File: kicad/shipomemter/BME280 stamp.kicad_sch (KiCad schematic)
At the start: 7 parts, among them U1 BME280

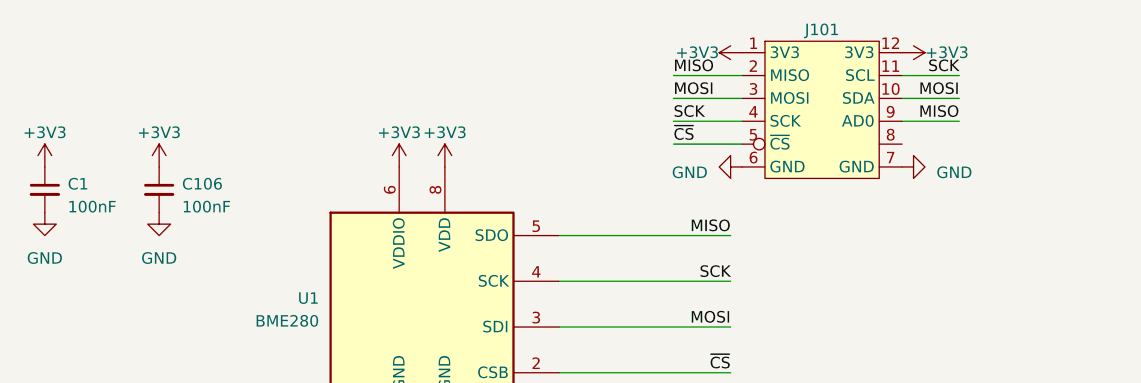
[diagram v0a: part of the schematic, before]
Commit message: Pulled in ICM20948
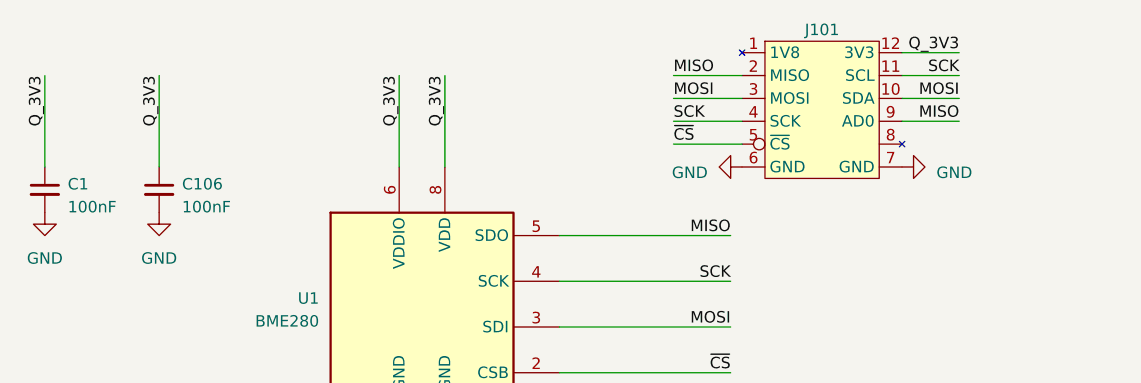
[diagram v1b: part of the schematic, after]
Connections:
- net +3V3 renamed Q_3V3
- net Q_3V3: no longer J101.1 (3V3)

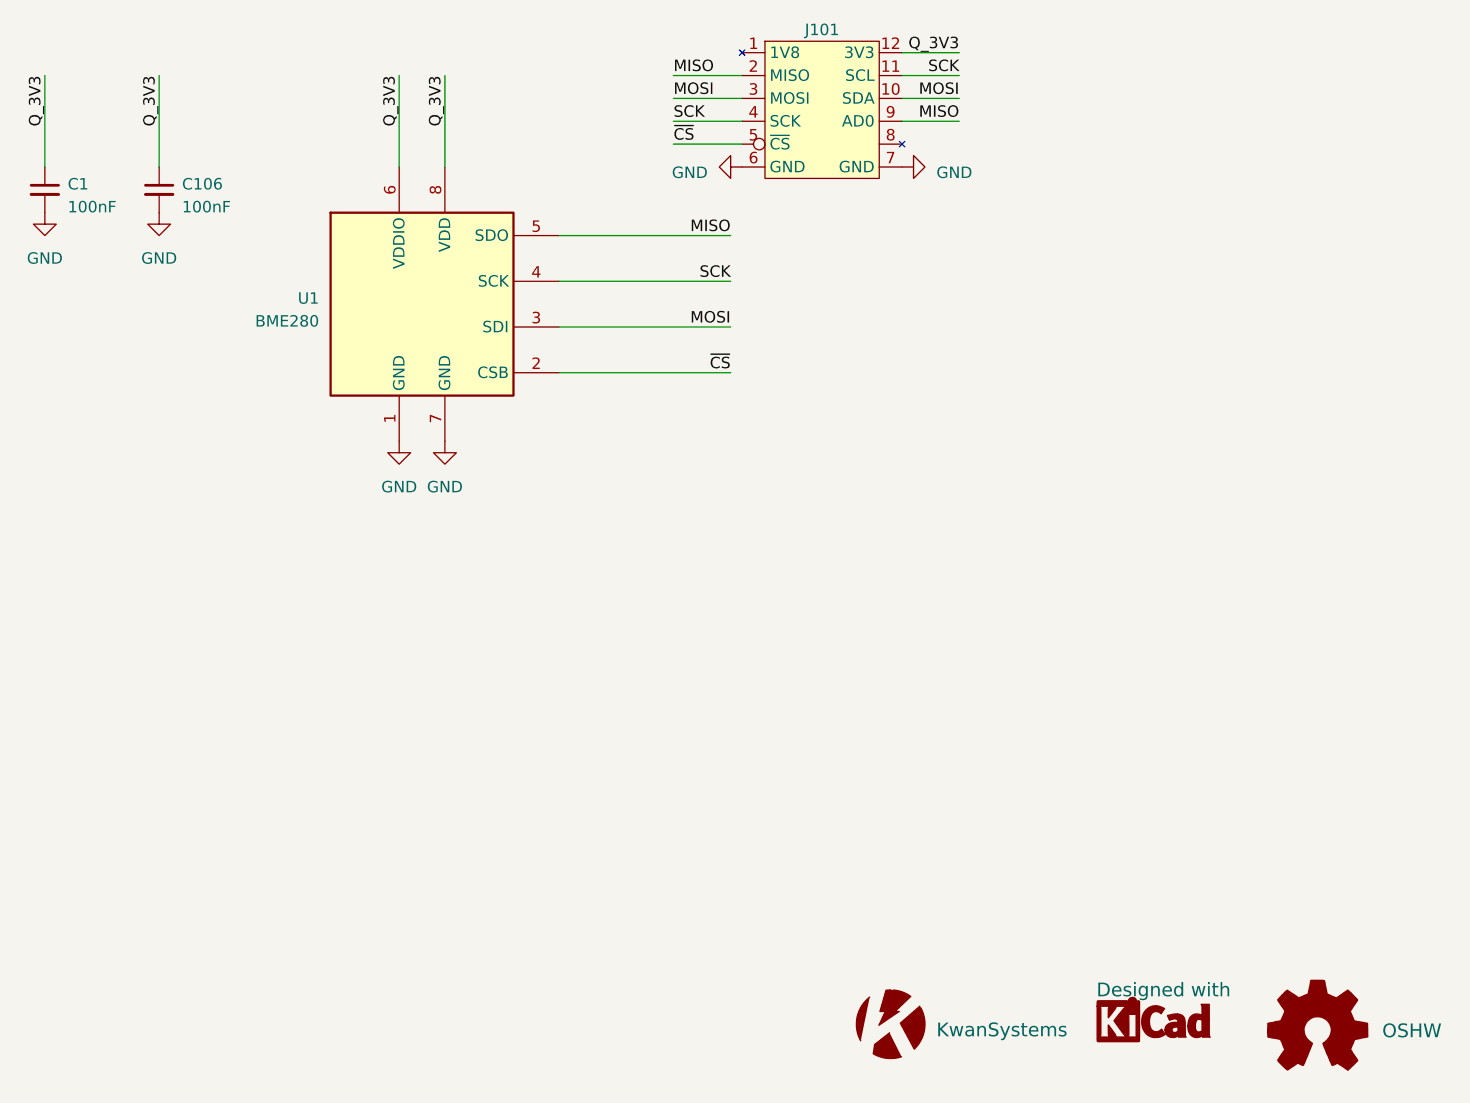
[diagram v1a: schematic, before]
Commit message: As ordered on 03 Apr 2023. Some but not all numbers-on-hand have been updated.
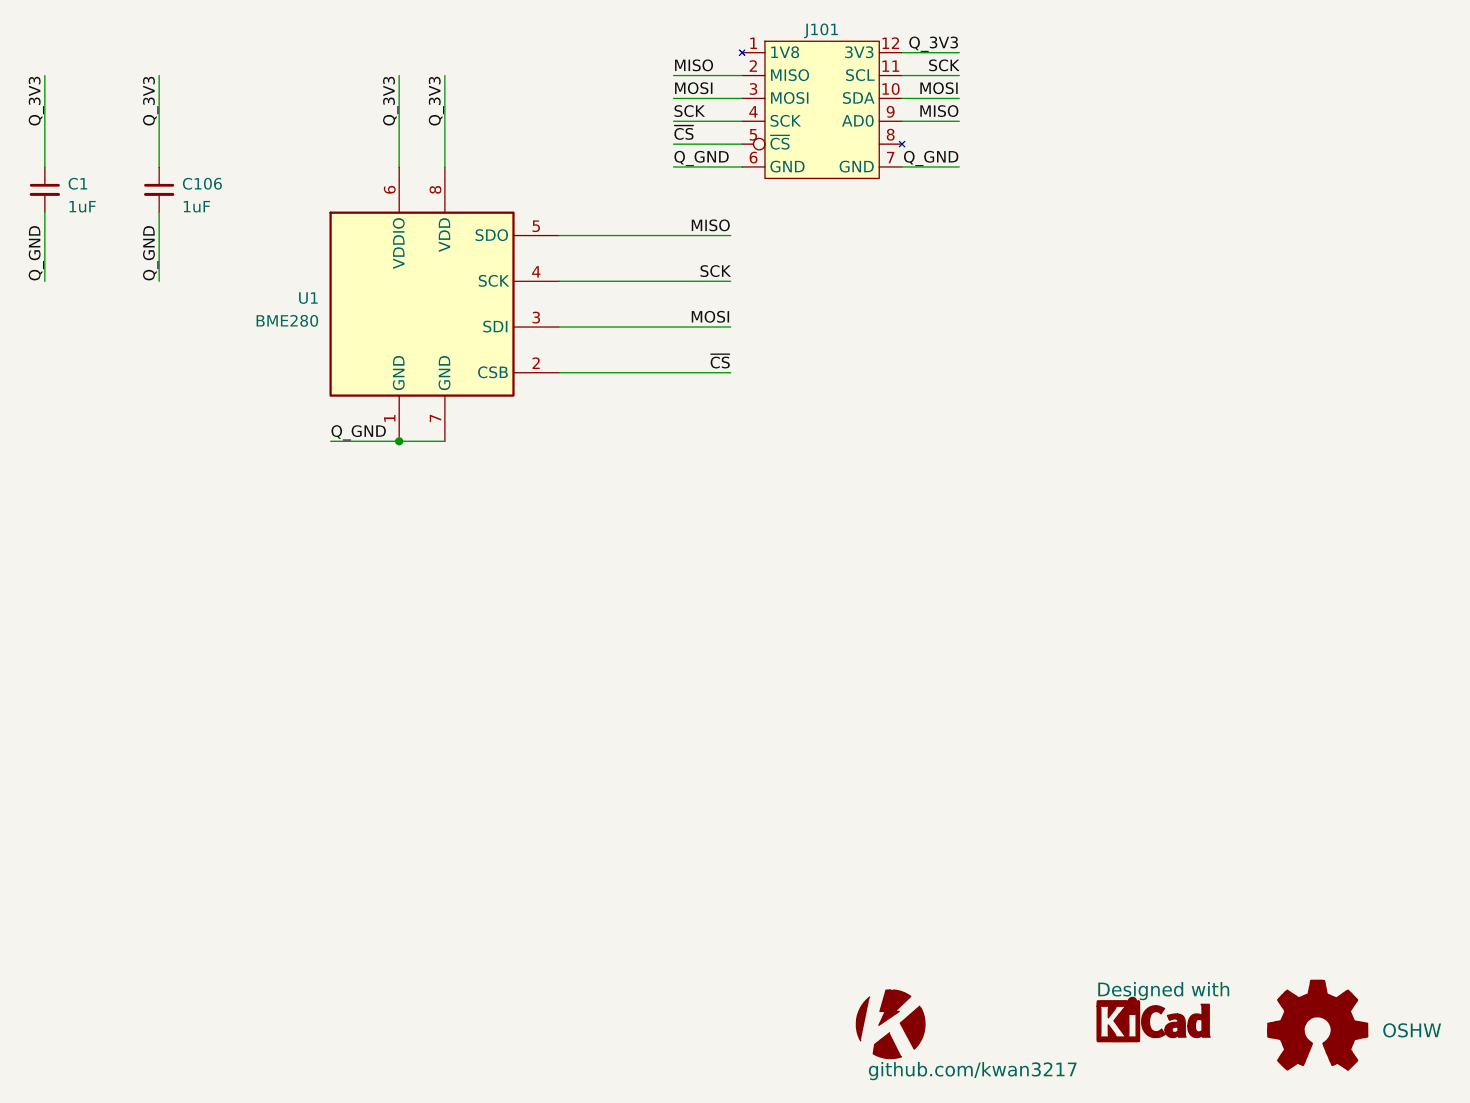
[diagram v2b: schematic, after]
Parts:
- C1, C106: value 100nF -> 1uF; Digikey (none) -> 399-C0603C105K4PAC7411CT-ND; Mouser (none) -> 80-C0603C105K4PAC
- G1: value KwanSystems -> github.com/kwan3217
- U1: Digikey (none) -> 828-1063-1-ND; Mouser (none) -> 262-BME280; Number in cart (none) -> 1; Number on hand (none) -> 0
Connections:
- net GND renamed Q_GND

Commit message: Updated numbers on hand and numbers in cart
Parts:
- C1, C106: Number in cart (none) -> 24; Number on hand (none) -> 0
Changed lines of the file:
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@@
+      (effects (font (size 1.27 1.27)) hide)
+    )
+    (property "Number in cart" "24" (at 88.9 78.74 0)
+      (effects (font (size 1.27 1.27)) hide)
+    )
+    (property "Number on hand" "0" (at 88.9 78.74 0)
       (effects (font (size 1.27 1.27)) hide)
     )
@@
       (effects (font (size 1.27 1.27)) hide)
     )
+    (property "Number in cart" "24" (at 101.6 78.74 0)
+      (effects (font (size 1.27 1.27)) hide)
+    )
+    (property "Number on hand" "0" (at 101.6 78.74 0)
+      (effects (font (size 1.27 1.27)) hide)
+    )

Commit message: Updated number on hand, and added more Digikey/Mouser/Mfg numbers
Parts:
- C1, C106: Number in cart 24 -> (none); Number on hand 0 -> 24; Part Number (none) -> C0603C105K4PAC
- U1: Number in cart 1 -> (none); Number on hand 0 -> 1; Part Number (none) -> BME280
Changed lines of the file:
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@@
       (effects (font (size 1.27 1.27)) hide)
     )
-    (property "Number in cart" "1" (at 130.81 91.44 0)
-      (effects (font (size 1.27 1.27)) hide)
-    )
-    (property "Number on hand" "0" (at 130.81 91.44 0)
+    (property "Number in cart" "" (at 130.81 91.44 0)
+      (effects (font (size 1.27 1.27)) hide)
+    )
+    (property "Number on hand" "1" (at 130.81 91.44 0)
       (effects (font (size 1.27 1.27)) hide)
     )
     (property "Mouser" "262-BME280" (at 130.81 91.44 0)
+      (effects (font (size 1.27 1.27)) hide)
+    )
+    (property "Part Number" "BME280" (at 130.81 91.44 0)
       (effects (font (size 1.27 1.27)) hide)
     )
@@
       (effects (font (size 1.27 1.27)) hide)
     )
-    (property "Number in cart" "24" (at 88.9 78.74 0)
-      (effects (font (size 1.27 1.27)) hide)
-    )
-    (property "Number on hand" "0" (at 88.9 78.74 0)
+    (property "Number in cart" "" (at 88.9 78.74 0)
+      (effects (font (size 1.27 1.27)) hide)
+    )
+    (property "Number on hand" "24" (at 88.9 78.74 0)
+      (effects (font (size 1.27 1.27)) hide)
+    )
+    (property "Part Number" "C0603C105K4PAC" (at 88.9 78.74 0)
       (effects (font (size 1.27 1.27)) hide)
     )
@@
       (effects (font (size 1.27 1.27)) hide)
     )
-    (property "Number in cart" "24" (at 101.6 78.74 0)
-      (effects (font (size 1.27 1.27)) hide)
-    )
-    (property "Number on hand" "0" (at 101.6 78.74 0)
-      (effects (font (size 1.27 1.27)) hide)
-    )
+    (property "Number in cart" "" (at 101.6 78.74 0)
+      (effects (font (size 1.27 1.27)) hide)
+    )
+    (property "Number on hand" "24" (at 101.6 78.74 0)
+      (effects (font (size 1.27 1.27)) hide)
+    )
+    (property "Part Number" "C0603C105K4PAC" (at 101.6 78.74 0)
+      (effects (font (size 1.27 1.27)) hide)
+    )

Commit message: Updated stuff that was needed to make Shipometer 23.04 case
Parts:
- C1, C106: Number on hand 24 -> 12
- U1: Number in cart (none) -> 1; Number on hand 1 -> 0
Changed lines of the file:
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@@
       (effects (font (size 1.27 1.27)) hide)
     )
-    (property "Number in cart" "" (at 130.81 91.44 0)
-      (effects (font (size 1.27 1.27)) hide)
-    )
-    (property "Number on hand" "1" (at 130.81 91.44 0)
+    (property "Number in cart" "1" (at 130.81 91.44 0)
+      (effects (font (size 1.27 1.27)) hide)
+    )
+    (property "Number on hand" "0" (at 130.81 91.44 0)
       (effects (font (size 1.27 1.27)) hide)
     )
@@
       (effects (font (size 1.27 1.27)) hide)
     )
-    (property "Number on hand" "24" (at 88.9 78.74 0)
+    (property "Number on hand" "12" (at 88.9 78.74 0)
       (effects (font (size 1.27 1.27)) hide)
     )
@@
       (effects (font (size 1.27 1.27)) hide)
     )
-    (property "Number on hand" "24" (at 101.6 78.74 0)
-      (effects (font (size 1.27 1.27)) hide)
-    )
+    (property "Number on hand" "12" (at 101.6 78.74 0)
+      (effects (font (size 1.27 1.27)) hide)
+    )
